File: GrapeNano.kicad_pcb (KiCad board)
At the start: 2 copper layers, 18.5 x 43.7 mm, 32 parts, among them P1 USB_OTG, P2 ICSP, SW1 SW_Push, U1 LM1117-5.0, U2 CH340C, U3 ATMEGA328P-AU, Y2 16Mhz

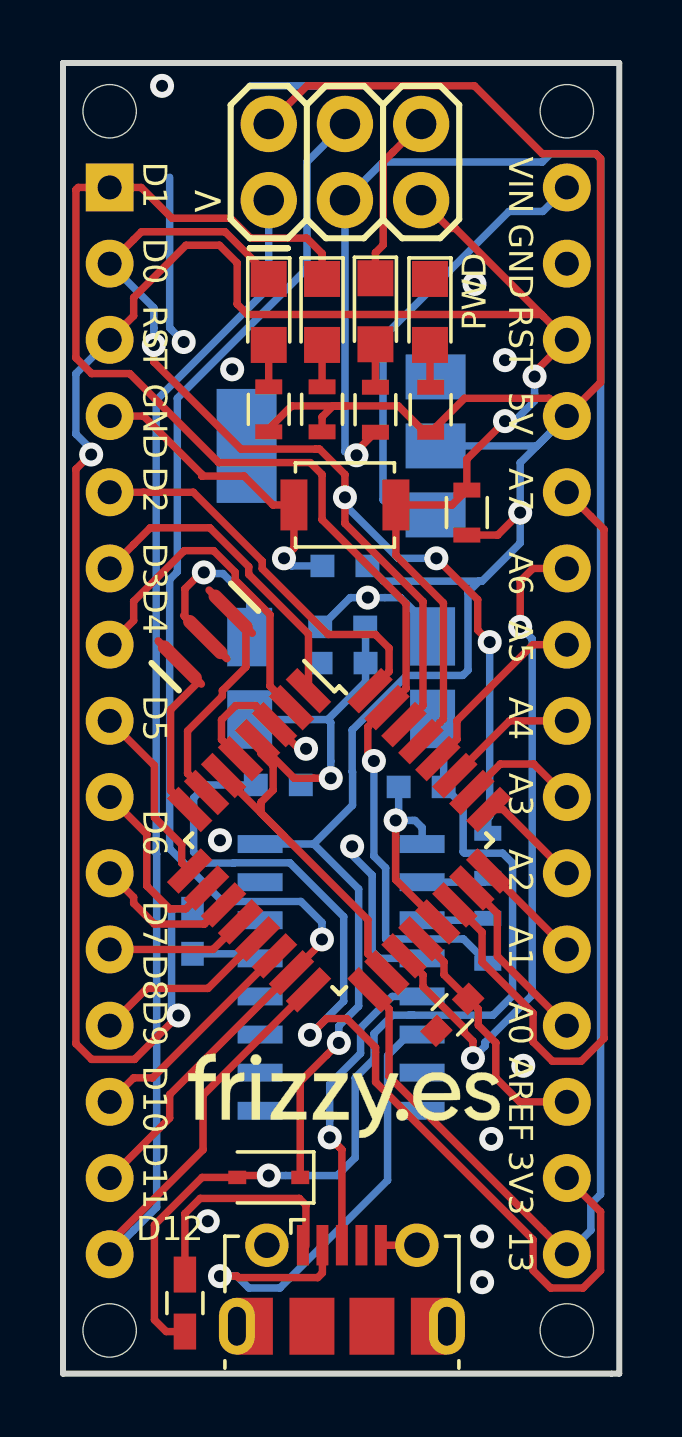
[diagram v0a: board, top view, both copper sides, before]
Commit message: Errores corregidos y mandado a fábrica
Corto en el condensador C1 y U3 sin alimentación
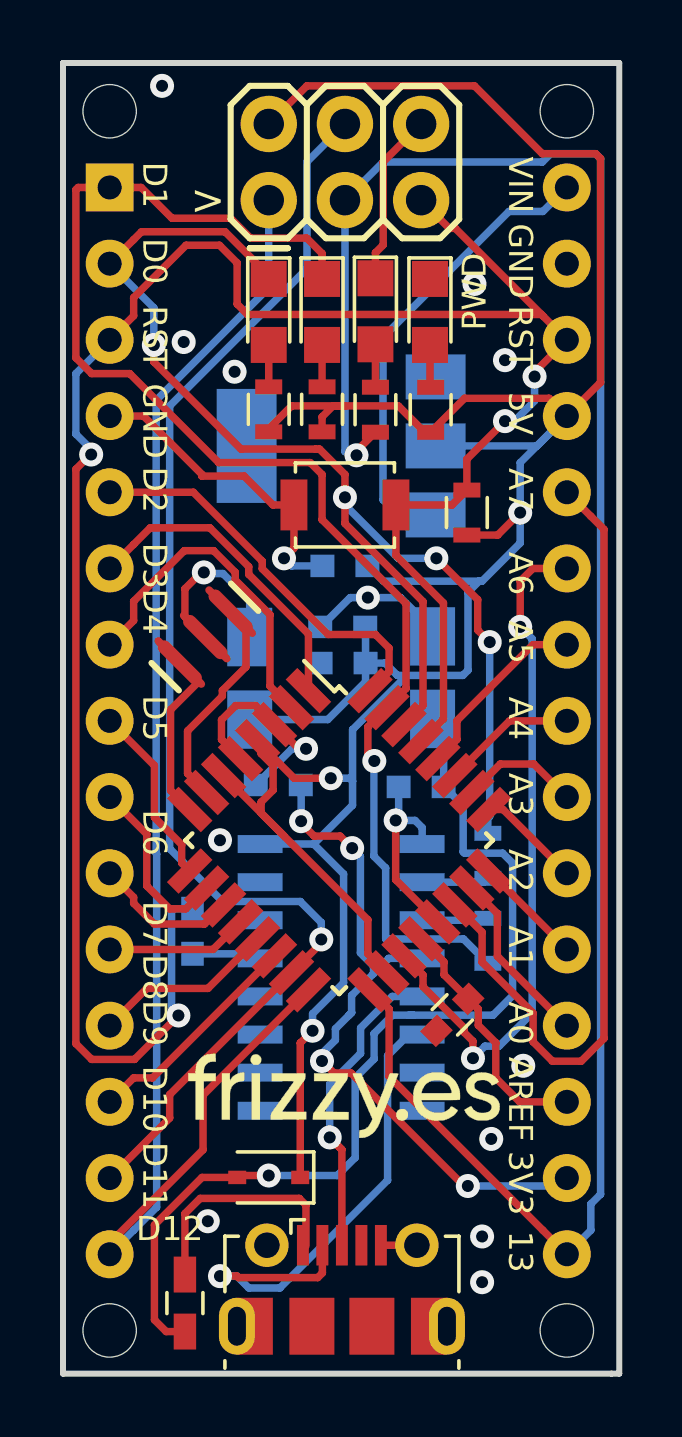
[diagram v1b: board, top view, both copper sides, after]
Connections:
- C1 pad 1: +3V3 -> GND
- C1 pad 2: GND -> +3V3
- C6 pad 1: Net-(C6-Pad1) -> +5V
- C7 pad 1: Net-(C6-Pad1) -> +5V
- C9 pad 1: Net-(C6-Pad1) -> +5V
- U2 pad 4: GND -> +3V3
- U3 pad 18: Net-(C6-Pad1) -> +5V
- U3 pad 4: Net-(C6-Pad1) -> +5V
- U3 pad 6: Net-(C6-Pad1) -> +5V
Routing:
- net Net-(C6-Pad1): track 23.8 -> 0.00 mm, vias 1 -> 0
- net +5V: track 78.6 -> 102.3 mm, vias 2 -> 3
- net +3V3: track 33.1 -> 23.4 mm, vias 1 -> 4
- net GND: track 51.4 -> 42.6 mm, vias 17 -> 16
- net (no net): track 4.16 -> 0.00 mm
